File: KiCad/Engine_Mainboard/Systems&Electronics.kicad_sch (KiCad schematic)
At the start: 39 parts, among them U13 AD8495, U14 AD8495, U15 AD8495, U16 AD8495, U3 MAX485E, U4 MAX485E

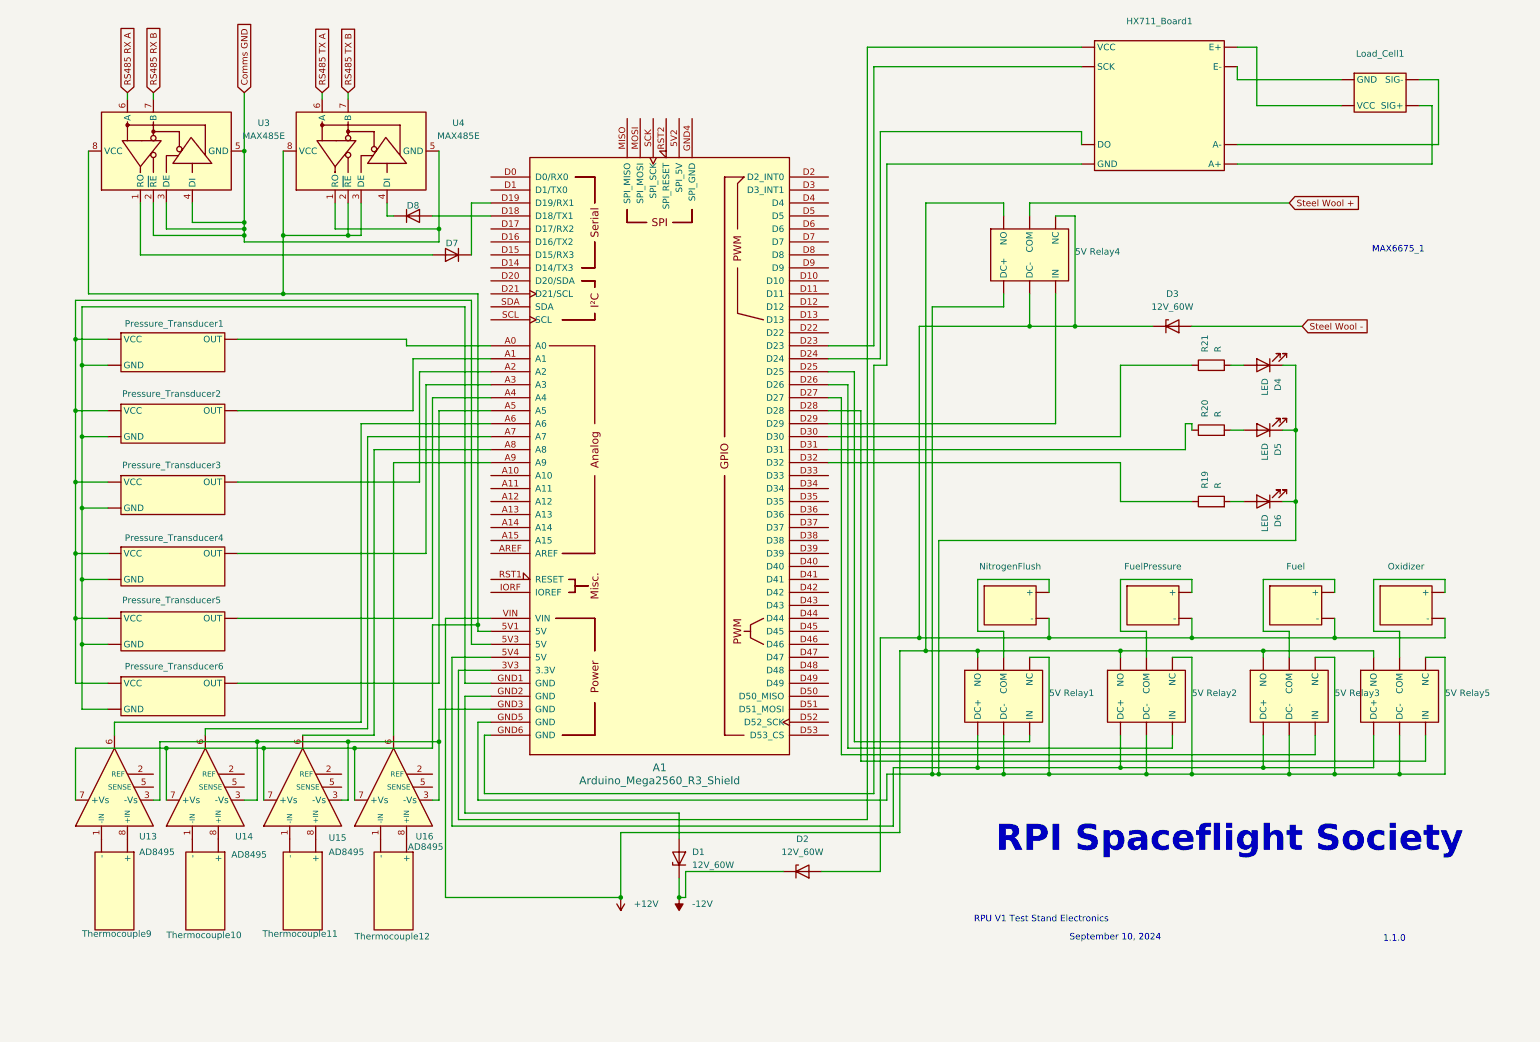
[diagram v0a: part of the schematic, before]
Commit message: feat(PCB): PCB V1.1.0 (#14)
* PCB Layout V1

* PCB layout minor updates

* Footprint and PCB updates

* PCB design reorg

* PCB Ignition Resistor Move

* PCB minor trace move
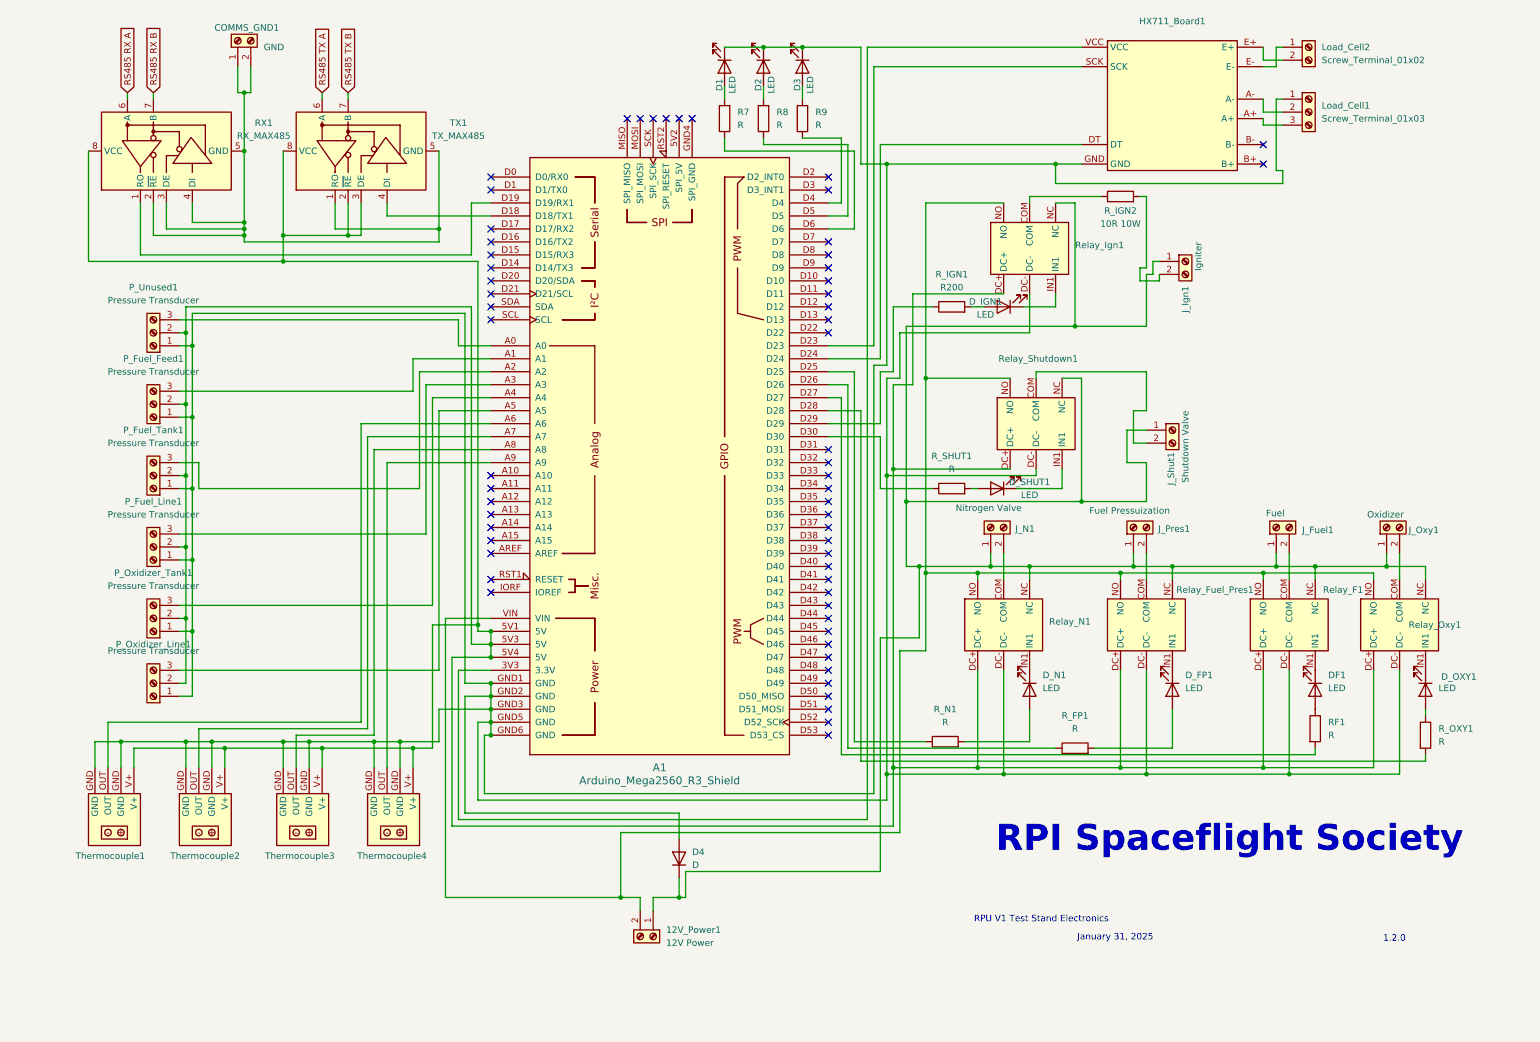
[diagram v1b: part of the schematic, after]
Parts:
- removed D1, D2, D3: 12V_60W, Diode_SMD:Nexperia_DSN1608-2_1.6x0.8mm, symbol Diode:PTVS12VZ1USK
- removed D4, D5, D6: LED, symbol Device:LED
- removed D7, D8: D, symbol Device:D
- removed Fuel, FuelPressure, NitrogenFlush, Oxidizer: ~, symbol Solenoids:Solenoid
- removed Load_Cell1: ~, symbol Sensors:Load_Cell
- removed Pressure_Transducer1, Pressure_Transducer2, Pressure_Transducer3, Pressure_Transducer4, Pressure_Transducer5, Pressure_Transducer6: ~, symbol Sensors:Pressure_Transducer
- removed R19, R20, R21: R, symbol Device:R
- removed Thermocouple10, Thermocouple11, Thermocouple12, Thermocouple9: ~, symbol Sensors:Thermocouple
- removed U13, U14, U15, U16: AD8495, Package_SO:MSOP-8_3x3mm_P0.65mm, symbol Sensor_Temperature:AD8495
- added 12V_Power1: 12V Power, TerminalBlock:TerminalBlock_bornier-2_P5.08mm, symbol Connector:Screw_Terminal_01x02
- added COMMS_GND1: GND, TerminalBlock:TerminalBlock_bornier-2_P5.08mm, symbol Connector:Screw_Terminal_01x02
- added D1, D2, D3, DF1, D_FP1, D_IGN1, D_N1, D_OXY1, D_SHUT1: LED, LED_THT:LED_D5.0mm, symbol Device:LED
- added D4: D, Diode_THT:D_A-405_P7.62mm_Horizontal, symbol Device:D
- added J_Fuel1: Fuel, TerminalBlock:TerminalBlock_bornier-2_P5.08mm, symbol Connector:Screw_Terminal_01x02
- added J_Ign1: Igniter, TerminalBlock:TerminalBlock_bornier-2_P5.08mm, symbol Connector:Screw_Terminal_01x02
- added J_N1: Nitrogen Valve, TerminalBlock:TerminalBlock_bornier-2_P5.08mm, symbol Connector:Screw_Terminal_01x02
- added J_Oxy1: Oxidizer, TerminalBlock:TerminalBlock_bornier-2_P5.08mm, symbol Connector:Screw_Terminal_01x02
- added J_Pres1: Fuel Pressuization, TerminalBlock:TerminalBlock_bornier-2_P5.08mm, symbol Connector:Screw_Terminal_01x02
- added J_Shut1: Shutdown Valve, TerminalBlock:TerminalBlock_bornier-2_P5.08mm, symbol Connector:Screw_Terminal_01x02
- added Load_Cell1: Screw_Terminal_01x03, TerminalBlock:TerminalBlock_bornier-3_P5.08mm, symbol Connector:Screw_Terminal_01x03
- added Load_Cell2: Screw_Terminal_01x02, TerminalBlock:TerminalBlock_bornier-2_P5.08mm, symbol Connector:Screw_Terminal_01x02
- added P_Fuel_Feed1, P_Fuel_Line1, P_Fuel_Tank1, P_Oxidizer_Line1, P_Oxidizer_Tank1, P_Unused1: Pressure Transducer, TerminalBlock:TerminalBlock_bornier-3_P5.08mm, symbol Connector:Screw_Terminal_01x03
- added R7, R8, R9, RF1, R_FP1, R_N1, R_OXY1, R_SHUT1: R, Resistor_THT:R_Axial_DIN0207_L6.3mm_D2.5mm_P7.62mm_Horizontal, symbol Device:R
- added R_IGN1: R200, Resistor_THT:R_Axial_DIN0207_L6.3mm_D2.5mm_P7.62mm_Horizontal, symbol Device:R
- added R_IGN2: 10R 10W, Resistor_THT:R_Axial_Power_L50.0mm_W9.0mm_P55.88mm, symbol Device:R
- added Relay_Shutdown1: ~, ValveControl:Relay, symbol 5VRelay:5V_Relay
- added Thermocouple1, Thermocouple2, Thermocouple3, Thermocouple4: ~, Sensors:AD8495, symbol Sensors:AD8495_PCB
- A1: footprint PCM_arduino-library:Arduino_Mega2560_R3_Shield -> Arduino:Arduino_Mega2560_R3_Shield
- HX711_Board1: footprint (none) -> Sensors:HX711
- RX1: renamed from U3; value MAX485E -> RX_MAX485; footprint Package_SO:SOIC-8_3.9x4.9mm_P1.27mm -> Communications:RS485_Transceiver
- Relay_F1: renamed from 5V Relay3; footprint (none) -> ValveControl:Relay
- Relay_Fuel_Pres1: renamed from 5V Relay2; footprint (none) -> ValveControl:Relay
- Relay_Ign1: renamed from 5V Relay4; footprint (none) -> ValveControl:Relay
- Relay_N1: renamed from 5V Relay1; footprint (none) -> ValveControl:Relay
- Relay_Oxy1: renamed from 5V Relay5; footprint (none) -> ValveControl:Relay
- TX1: renamed from U4; value MAX485E -> TX_MAX485; footprint Package_SO:SOIC-8_3.9x4.9mm_P1.27mm -> Communications:RS485_Transceiver
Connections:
- net at A1.D28: now also R_OXY1.2; no longer Relay_Oxy1. (NO)
- net at A1.D25: now also R_N1.1; no longer Relay_N1. (NO)
- net at A1.D30: now also R_SHUT1.1
- net at A1.3V3 (3.3V): now also HX711_Board1.VCC; no longer HX711_Board1. (VCC)
- net at A1.5V1 (5V), RX1.8 (VCC), TX1.2 (~{RE})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: now also A1.5V3 (5V), A1.5V4 (5V), Relay_F1.DC+, Relay_Fuel_Pres1.DC+, Relay_Ign1.DC+, Relay_N1.DC+, Relay_Oxy1.DC+, P_Fuel_Feed1.2 (Pin_2), P_Fuel_Line1.2 (Pin_2), P_Fuel_Tank1.2 (Pin_2), P_Oxidizer_Line1.2 (Pin_2), P_Oxidizer_Tank1.2 (Pin_2), P_Unused1.2 (Pin_2), Relay_Shutdown1.DC+, Thermocouple1.V+, Thermocouple2.V+, Thermocouple3.V+, Thermocouple4.V+
- net at A1.A0: now also P_Unused1.3 (Pin_3)
- net at A1.A1: now also P_Fuel_Feed1.3 (Pin_3)
- net at A1.A2: now also P_Fuel_Tank1.3 (Pin_3)
- net at A1.A3: now also P_Fuel_Line1.3 (Pin_3)
- net at A1.A4: now also P_Oxidizer_Tank1.3 (Pin_3)
- net at A1.A5: now also P_Oxidizer_Line1.3 (Pin_3)
- net at A1.A6: now also Thermocouple1.OUT
- net at A1.A7: now also Thermocouple2.OUT
- net at A1.A8: now also Thermocouple3.OUT
- net at A1.A9: now also Thermocouple4.OUT
- net at A1.D18 (D18/TX1): now also TX1.4 (DI)
- net at A1.D19 (D19/RX1): now also RX1.1 (RO)
- net at A1.D23: now also HX711_Board1.SCK; no longer HX711_Board1. (VCC)
- net at A1.D24: now also HX711_Board1.DT; no longer HX711_Board1. (VCC)
- net at A1.D26: now also R_FP1.1; no longer Relay_Fuel_Pres1. (NO)
- net at A1.D27: now also RF1.2; no longer Relay_F1. (NO)
- net at A1.D29: now also R_IGN1.1; no longer Relay_Ign1. (NO)
- net at A1.D4: now also R9.1
- net at A1.D5: now also R8.1
- net at A1.D6: now also R7.1
- net at A1.GND1 (GND): now also A1.GND2 (GND), A1.GND3 (GND), A1.GND5 (GND), A1.GND6 (GND), HX711_Board1.GND, Relay_F1.DC-, Relay_Fuel_Pres1.DC-, Relay_Ign1.DC-, Relay_N1.DC-, Relay_Oxy1.DC-, D1.1 (K), D2.1 (K), D3.1 (K), D4.2 (A), Load_Cell1.1 (Pin_1), P_Fuel_Feed1.1 (Pin_1), P_Fuel_Line1.1 (Pin_1), P_Fuel_Tank1.1 (Pin_1), P_Oxidizer_Line1.1 (Pin_1), P_Oxidizer_Tank1.1 (Pin_1), P_Unused1.1 (Pin_1), Relay_Shutdown1.DC-, Thermocouple1.GND, Thermocouple2.GND, Thermocouple3.GND, Thermocouple4.GND
- removed net +12V: A1.VIN, Relay_F1. (NO), Relay_Fuel_Pres1. (NO), Relay_Ign1. (NO), Relay_N1. (NO), Relay_Oxy1. (NO)
- net Comms GND: no longer names the net of RX1.2 (~{RE}), RX1.3 (DE), RX1.4 (DI), RX1.5 (GND), TX1.1 (RO), TX1.5 (GND)
- net Comms GND: now also COMMS_GND1.1 (Pin_1), COMMS_GND1.2 (Pin_2)
- removed net Steel Wool +: Relay_Ign1. (NO)
- new net: 12V_Power1.1 (Pin_1), D4.1 (K), J_Fuel1.1 (Pin_1), J_Ign1.1 (Pin_1), J_N1.1 (Pin_1), J_Oxy1.1 (Pin_1), J_Pres1.1 (Pin_1), J_Shut1.1 (Pin_1), Relay_F1.NC, Relay_Fuel_Pres1.NC, Relay_Ign1.NC, Relay_N1.NC, Relay_Oxy1.NC, Relay_Shutdown1.NC
- new net: J_N1.2 (Pin_2), Relay_N1.COM
- new net: J_Oxy1.2 (Pin_2), Relay_Oxy1.COM
- new net: D_OXY1.1 (K), Relay_Oxy1.IN1
- new net: 12V_Power1.2 (Pin_2), A1.VIN, Relay_F1.NO, Relay_Fuel_Pres1.NO, Relay_Ign1.NO, Relay_N1.NO, Relay_Oxy1.NO, Relay_Shutdown1.NO
- new net: D_IGN1.2 (A), R_IGN1.2
- new net: D_N1.1 (K), Relay_N1.IN1
- new net: DF1.2 (A), RF1.1
- new net: D_FP1.1 (K), Relay_Fuel_Pres1.IN1
- new net: D_FP1.2 (A), R_FP1.2
- new net: D_SHUT1.2 (A), R_SHUT1.2
- new net: D_SHUT1.1 (K), Relay_Shutdown1.IN1
- new net: D1.2 (A), R7.2
- new net: J_Shut1.2 (Pin_2), Relay_Shutdown1.COM
- new net: D_N1.2 (A), R_N1.2
- new net: J_Pres1.2 (Pin_2), Relay_Fuel_Pres1.COM
- new net: D2.2 (A), R8.2
- new net: R_IGN2.1, Relay_Ign1.COM
- new net: D_IGN1.1 (K), Relay_Ign1.IN1
- new net: D3.2 (A), R9.2
- new net: HX711_Board1.E-, Load_Cell2.1 (Pin_1)
- new net: HX711_Board1.E+, Load_Cell2.2 (Pin_2)
- new net: J_Fuel1.2 (Pin_2), Relay_F1.COM
- new net: DF1.1 (K), Relay_F1.IN1
- new net: D_OXY1.2 (A), R_OXY1.1
- new net: HX711_Board1.A+, Load_Cell1.3 (Pin_3)
- new net: HX711_Board1.A-, Load_Cell1.2 (Pin_2)
- new net: J_Ign1.2 (Pin_2), R_IGN2.2
- no-connect marks 0 -> 60
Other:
- note added: "1.2.0"
- note added: "January 31, 2025"
- note removed: "1.1.0"
- note removed: "MAX6675_1"
- note removed: "September 10, 2024"

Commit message: Finishing touches, added redundant power terminals, and reset button.
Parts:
- added 12V_Power2: 12V Aux Power, TerminalBlock:TerminalBlock_bornier-2_P5.08mm, symbol Connector:Screw_Terminal_01x02
- added R1: R, Resistor_THT:R_Axial_DIN0207_L6.3mm_D2.5mm_P7.62mm_Horizontal, symbol Device:R
- added RESET1: Reset, Button_Switch_THT:SW_PUSH_6mm, symbol Switch:SW_Push
- added RESET_ENABLE1: Jumper_2_Open, Connector_PinHeader_2.54mm:PinHeader_1x02_P2.54mm_Vertical, symbol Jumper:Jumper_2_Open
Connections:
- net at 12V_Power1.1 (Pin_1), D4.1 (K), J_Fuel1.1 (Pin_1)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: now also 12V_Power2.1 (Pin_1)
- net at A1.GND1 (GND), A1.GND2 (GND), A1.GND3 (GND)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: now also RESET1.1
- net at A1.5V1 (5V), A1.5V3 (5V), A1.5V4 (5V)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: now also R1.2
- net at 12V_Power1.2 (Pin_2), A1.VIN, Relay_F1.NO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: now also 12V_Power2.2 (Pin_2)
- net at A1.RST1 (RESET): now also R1.1, RESET_ENABLE1.2 (B)
- new net: RESET1.2, RESET_ENABLE1.1 (A)
- no-connect marks 60 -> 59
